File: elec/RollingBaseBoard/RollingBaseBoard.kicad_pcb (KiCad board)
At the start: 2 copper layers, 80 x 80 mm, 102 parts, among them P1 GP2, P10 UART_2, P11 I2C, P12 Motor, P13 Motor, P14 Encoder2, P15 Motor, P16 Switch, P17 Switch, P18 Switch, P19 Switch, P2 GP2, P20 Switch, P3 GP2, P4 GP2, P5 Bat5V, P6 Bat15V, P7 Encoder, P8 Encoder, P9 UART_1, U1 LMD18201, U2 LMD18201, U3 Teensy3.1

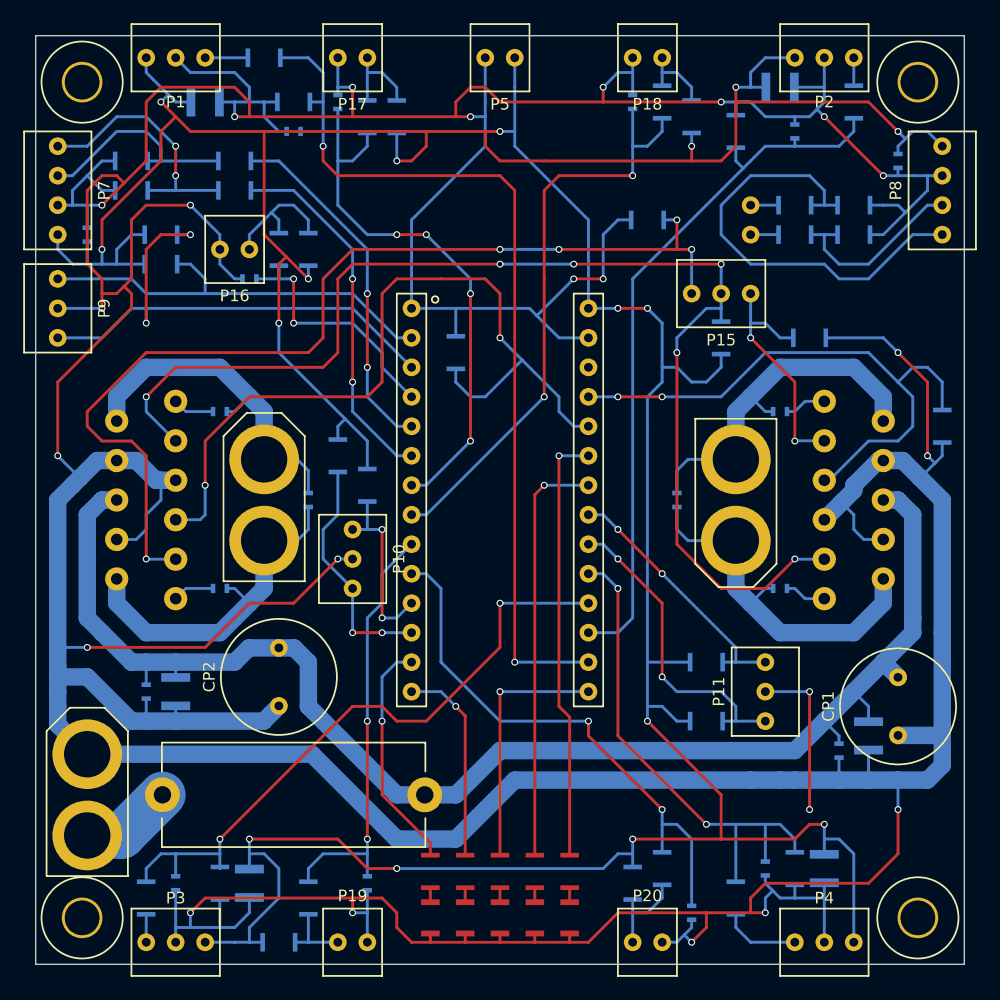
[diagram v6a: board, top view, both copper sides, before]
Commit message: Fixing rolling base board routing's right angles
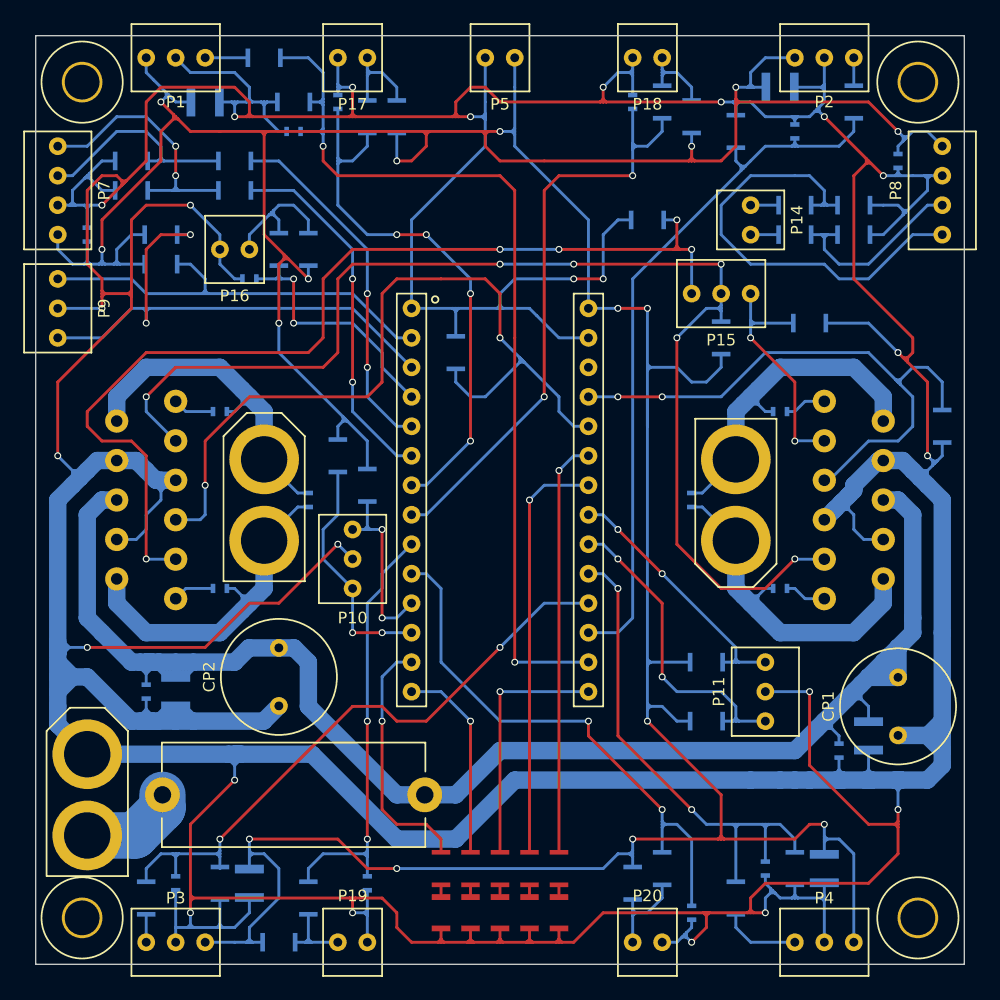
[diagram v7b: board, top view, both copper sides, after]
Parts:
- moved R24 1.27 mm to (175.2, 89.8)
- moved C13 1.27 mm to (165.0, 105.0)
- moved D1 1.02 mm to (143.4, 140.6)
- moved D5 1.02 mm to (153.6, 140.6)
- moved R28 0.95 mm to (143.4, 136.8)
- moved R32 0.95 mm to (153.6, 136.8)
- moved D2 0.64 mm to (146.0, 140.6)
- moved D4 0.64 mm to (151.0, 140.6)
- moved R29 0.52 mm to (146.0, 136.8)
- moved R31 0.52 mm to (151.0, 136.8)
- moved D3 0.44 mm to (148.5, 140.6)
- moved R30 0.25 mm to (148.5, 136.8)
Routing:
- net /Com/GND: track 666.2 -> 795.0 mm
- net /Driver_1/+15V: track 122.3 -> 151.3 mm
- net /Com/+5V: track 355.5 -> 372.5 mm
- net (no net): track 0.00 -> 2.54 mm
- net Net-(R28-Pad1): track 20.1 -> 21.8 mm
- net /Teensy/GP2_2: track 61.7 -> 63.2 mm
- net /Teensy/GP2_4: track 44.0 -> 45.4 mm
- net /Teensy/GP2_1: track 79.5 -> 80.9 mm
- net Net-(C18-Pad2): track 31.0 -> 32.4 mm
- net Net-(C18-Pad1): track 30.2 -> 31.6 mm
- net Net-(R32-Pad1): track 37.3 -> 36.0 mm
- net /Teensy/GP2_3: track 56.1 -> 55.3 mm
- net /Driver_2/PWM: track 69.3 -> 70.0 mm
- net Net-(P16-Pad2): track 11.1 -> 11.9 mm
- net /Driver_1/PWM: track 50.5 -> 51.2 mm
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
